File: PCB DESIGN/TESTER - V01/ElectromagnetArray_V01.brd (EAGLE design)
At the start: 77.5 x 100 mm, 44 parts, among them J1 POWER_JACKPTH_LOCK, Q1 IRLB3813, Q2 IRLB3813, Q3 IRLB3813, Q4 IRLB3813

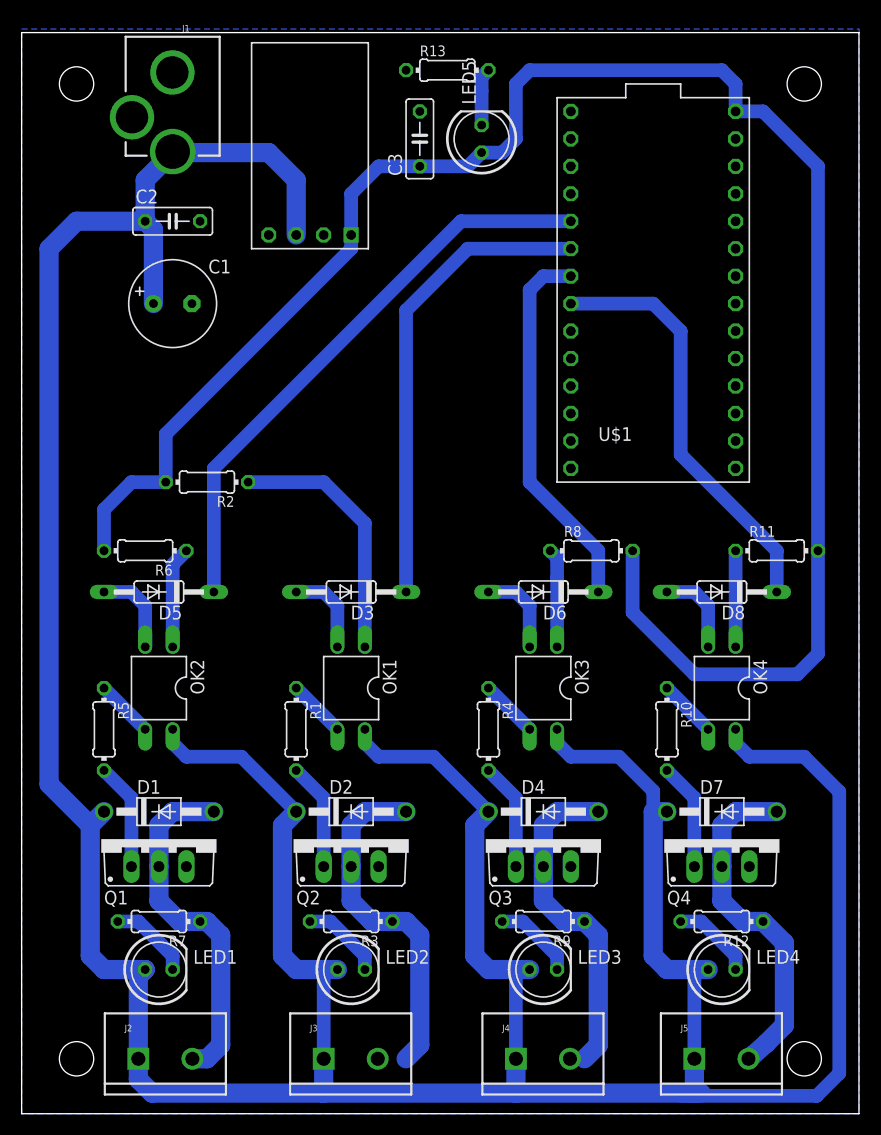
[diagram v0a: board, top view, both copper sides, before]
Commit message: Updates to Preliminary Design
Added pull down resistors for the Gate Input on the Transistors.
All opto isolator LEDs are on the 3V3 rail
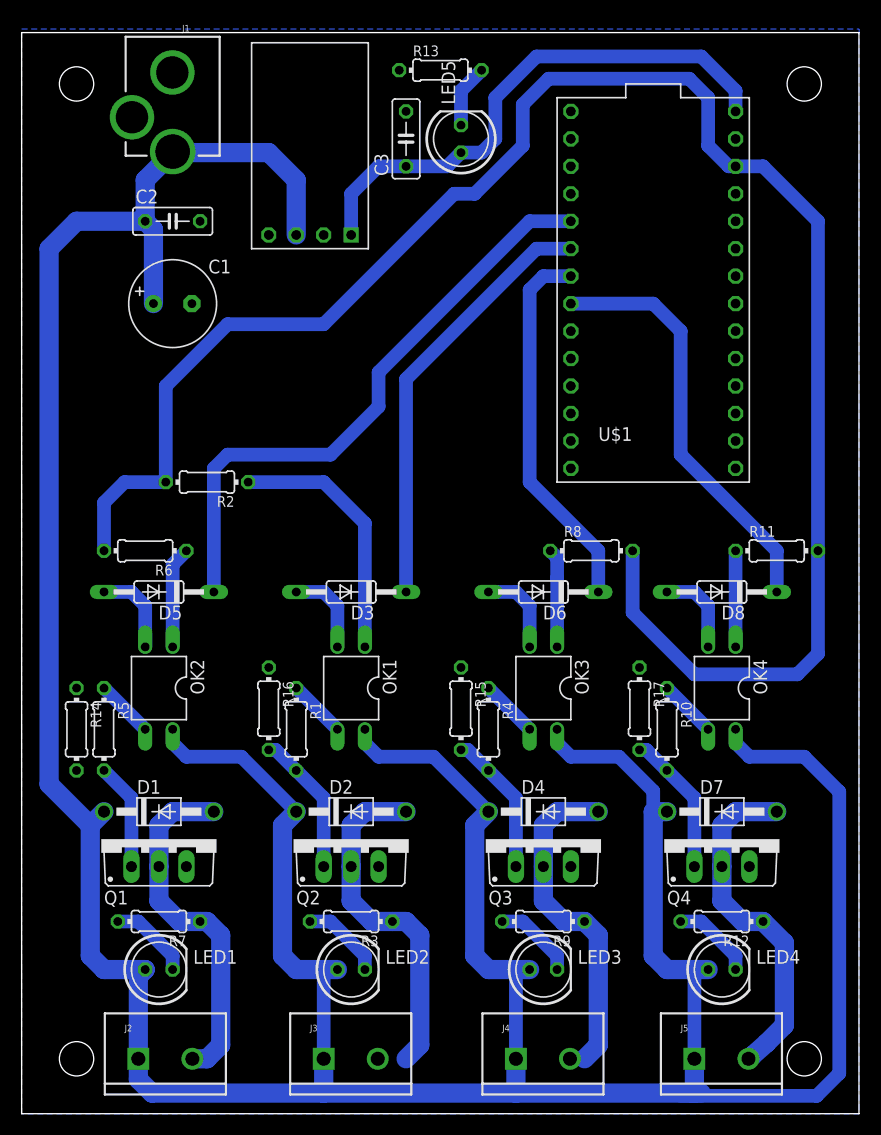
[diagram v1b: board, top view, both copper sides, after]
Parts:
- added R14, R15, R16, R17: 1k, rcl:0204/7
- moved LED5 1.91 mm to (40.6, 90.2)
- moved C3 1.27 mm to (35.6, 90.2)
- moved R13 0.63 mm to (38.7, 96.5)
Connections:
- removed net N$18: Q3.G, R4.2
- new net +3V3: R11.2, R2.2, R6.2, R8.2, U$1.26
- new net N$26: Q3.G, R15.2, R4.2
- net GND: now also R14.1, R15.1, R16.1, R17.1
- net N$1: now also R14.2
- net N$24: now also R17.2
- net N$7: now also R16.2
- net V_USB: no longer R11.2, R2.2, R6.2, R8.2
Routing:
- net +3V3: track 0.00 -> 168.3 mm
- net V_USB: track 171.5 -> 50.1 mm
- net N$26: track 0.00 -> 13.3 mm
- net N$18: track 9.94 -> 0.00 mm
- net D04: track 43.6 -> 39.9 mm
- net N$7: track 9.94 -> 13.3 mm
- net N$24: track 9.94 -> 13.3 mm
- net D03: track 53.9 -> 55.8 mm
- net N$25: track 5.34 -> 5.87 mm
